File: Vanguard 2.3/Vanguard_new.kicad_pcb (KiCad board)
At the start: 4 copper layers, 42.1 x 52.7 mm, 88 parts, among them J1 USB_C_Receptacle_USB2.0_16P, J2 Conn_02x03_Pin, J3 Micro_SD_Card_Det1, J4 STARBOARD_SERVO, J5 PORTSIDE_SERVO, J6 Battery In, J7 EJECTION_SERVO, Q1 BSS138, Q2 BSS138, Q3 BSS138, Q4 BSS138, U1 ATSAMD11D14A-M, U2 ATmega4809-A, U3 AT25DF641A-SH-T, U4 AP2112K-3.3, U5 BD1020HFV, U6 BNO086, U7 TXB0104D, U8 TPS61092, U9 MPM3610AGQV-P, Y1 32.768kHz

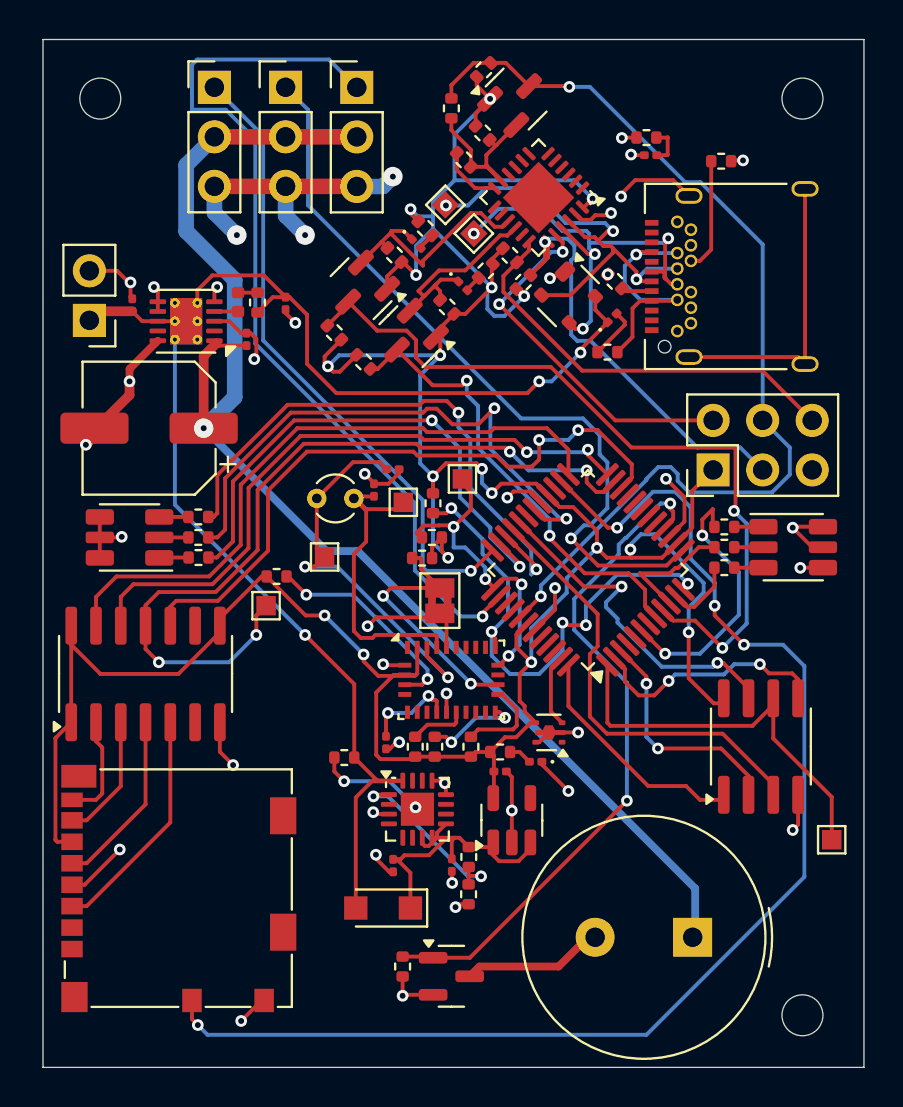
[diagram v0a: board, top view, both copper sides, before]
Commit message: removed usbc shield hybrid ground + small changes
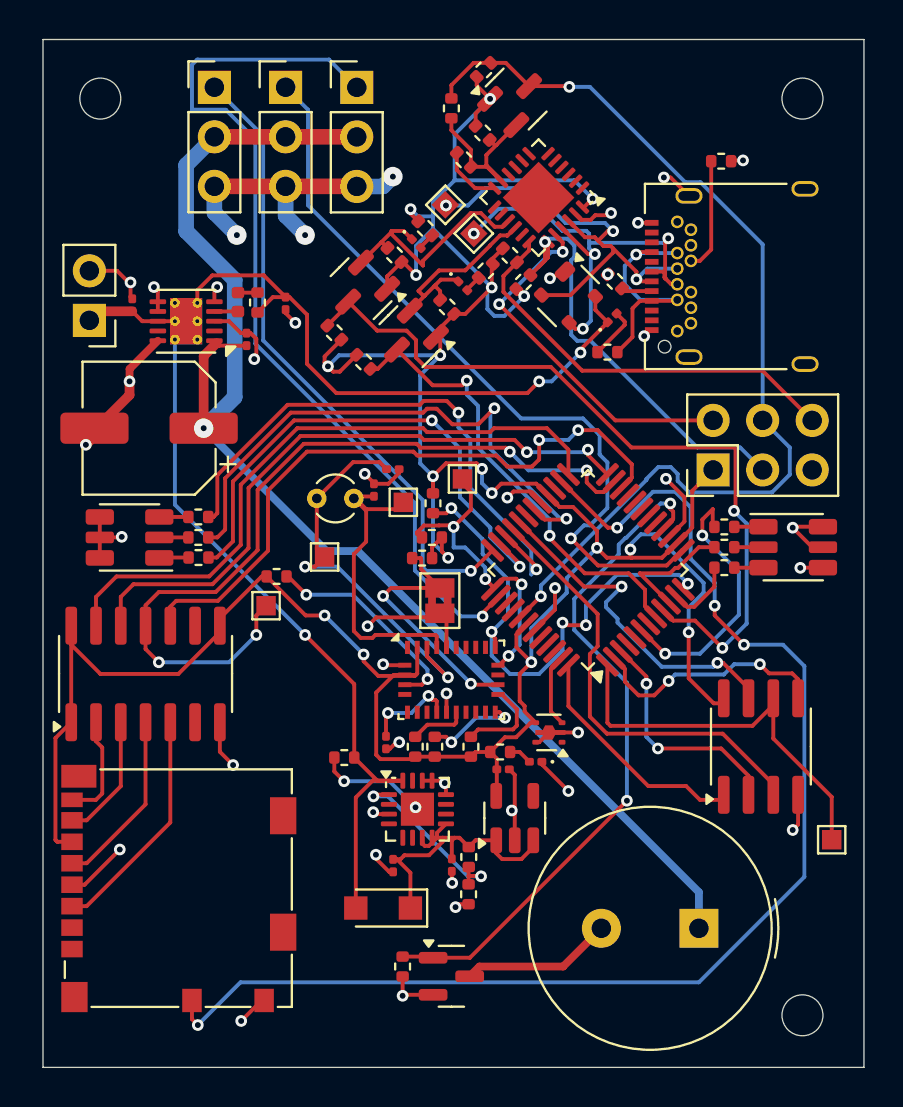
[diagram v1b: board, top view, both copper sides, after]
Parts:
- removed C1: 4n7, Capacitor_SMD:C_0201_0603Metric
- removed R1: 1M, Resistor_SMD:R_0402_1005Metric
- moved BZ1 0.56 mm to (126.2, 129.5)
- moved C6 0.19 mm to (116.2, 121.4)
- moved U4 0.19 mm to (116.8, 123.9)
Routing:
- net GND: track 111.0 -> 91.6 mm

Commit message: fiverr corrections
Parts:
- moved R21 14.5 mm to (126.4, 111.9), turned to 135 degrees
- moved R22 0.95 mm to (113.5, 109.5), turned to 0 degrees
- moved STARBOARD_RGB1 0.41 mm to (131.4, 110.1)
- moved R25 0.41 mm to (127.9, 109.0)
- moved R27 0.41 mm to (127.9, 111.1)
- moved R26 0.41 mm to (127.9, 110.1)
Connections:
- J1 pad A4: Net-(J1-VBUS-PadA4) -> BATT_IN
- J1 pad A9: Net-(J1-VBUS-PadA4) -> BATT_IN
- J1 pad B4: Net-(J1-VBUS-PadA4) -> BATT_IN
- J1 pad B9: Net-(J1-VBUS-PadA4) -> BATT_IN
- Q4 pad 3: Net-(BZ1--) -> unconnected-(Q4-D-Pad3)
- R35 pad 2: Net-(J1-VBUS-PadA4) -> BATT_IN
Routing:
- net Net-(J1-VBUS-PadA4): track 12.8 -> 0.00 mm, vias 1 -> 0
- net BATT_IN: track 74.5 -> 87.3 mm, vias 3 -> 4
- net SDA: track 25.7 -> 16.2 mm, vias 5 -> 4
- net PORT_BLUE: track 27.1 -> 24.0 mm
- net SCL: track 16.5 -> 13.9 mm
- net STAR_RED: track 6.54 -> 5.17 mm
- net STAR_BLUE: track 13.6 -> 12.3 mm
- net HOLD: track 17.8 -> 16.5 mm
- net +3.3V: track 169.6 -> 168.7 mm, vias 18 -> 19
- net UPDI: track 51.8 -> 52.7 mm
- net STAR_GREEN: track 3.58 -> 4.22 mm
- net CD: track 66.9 -> 66.3 mm, vias 4 -> 2
- net BUZZER: track 35.2 -> 34.7 mm

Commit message: wiring, fiverr, etc
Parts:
- BZ1: footprint Buzzer_Beeper:Buzzer_TDK_PS1240P02BT_D12.2mm_H6.5mm -> Buzzer_Beeper:MagneticBuzzer_Kingstate_KCG0601
- moved C4 24.0 mm to (108.2, 121.3)
- moved BZ1 3.65 mm to (122.6, 128.8)
- moved TP3 2.74 mm to (103.7, 115.7)
- moved REF** 2.45 mm to (131.0, 131.6)
- moved R24 1.63 mm to (104.2, 113.1)
- moved R14 1.25 mm to (109.1, 121.4), turned to -90 degrees
- moved D7 0.98 mm to (121.3, 99.1), turned to 180 degrees
- moved D6 0.54 mm to (110.4, 128.2)
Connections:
- BZ1 pad 1: +5V -> Net-(BZ1-+)
- BZ1 pad 2: Net-(BZ1--) -> GND
- Q4 pad 3: unconnected-(Q4-D-Pad3) -> Net-(BZ1-+)
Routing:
- net +5V: track 68.1 -> 31.0 mm
- net Net-(BZ1-+): track 0.00 -> 9.50 mm
- net GND: track 91.8 -> 82.9 mm, vias 41 -> 42
- net Net-(BZ1--): track 7.77 -> 0.00 mm
- net BATT_IN: track 87.3 -> 94.0 mm
- net Net-(ADR1-B): track 13.2 -> 10.6 mm
- net D4: track 41.4 -> 38.9 mm
- net Net-(U6-XOUT32/CLKSEL1): track 16.3 -> 13.8 mm
- net CD: track 66.3 -> 68.4 mm
- net Net-(D7-A): track 2.73 -> 0.88 mm
- net +3.3V: track 168.7 -> 167.2 mm, vias 19 -> 21
- net Net-(D6-K): track 16.1 -> 17.4 mm
- net PA0/MISO: track 12.0 -> 13.1 mm
- net HOLD: track 16.5 -> 17.6 mm
- net SCL: track 13.9 -> 12.9 mm
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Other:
- board size 42.1 x 52.7 mm -> 42.1 x 51.9 mm

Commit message: @Zumar-shariff
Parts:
- added C12: 4n7, Capacitor_SMD:C_0201_0603Metric, F.Cu at (94.0, 101.0)
- added C13: 100n, Capacitor_SMD:C_0201_0603Metric, F.Cu at (93.3, 101.0)
- U9: footprint Package_DFN_QFN:QFN-16-1EP_3x3mm_P0.5mm_EP1.7x1.7mm -> Package_DFN_QFN:QFN-20-1EP_4x4mm_P0.5mm_EP2.5x2.5mm_ThermalVias
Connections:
- C4 pad 1: BATT_IN -> Net-(U9-IN)
- J1 pad S1: GND -> unconnected-(J1-SHIELD-PadS1)
- R14 pad 1: BATT_IN -> Net-(U9-IN)
- U9 pad 16: BATT_IN -> Net-(U9-IN)
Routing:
- net BATT_IN: track 94.0 -> 100.4 mm
- net unconnected-(J1-SHIELD-PadS1): track 0.00 -> 1.68 mm, vias 0 -> 1
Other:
- board size 42.1 x 51.9 mm -> 42.3 x 51.9 mm
